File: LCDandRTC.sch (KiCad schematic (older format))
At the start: 13 parts, among them P6 2x8 socket strip, Q3 TSM2314, U2 PCA9306, U3 DS1338, X1 32.768kHz

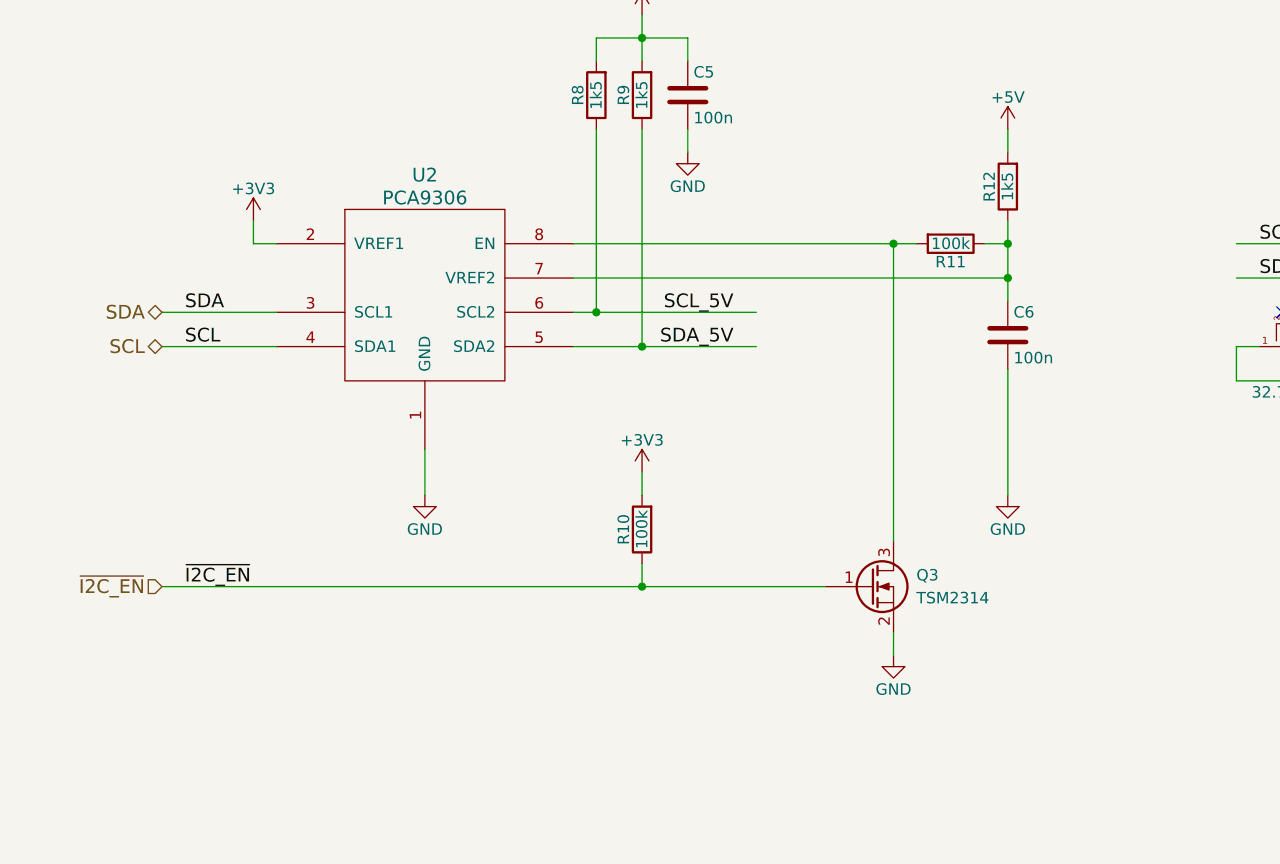
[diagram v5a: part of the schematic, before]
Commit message: Changed layout of I2C buffer enabling
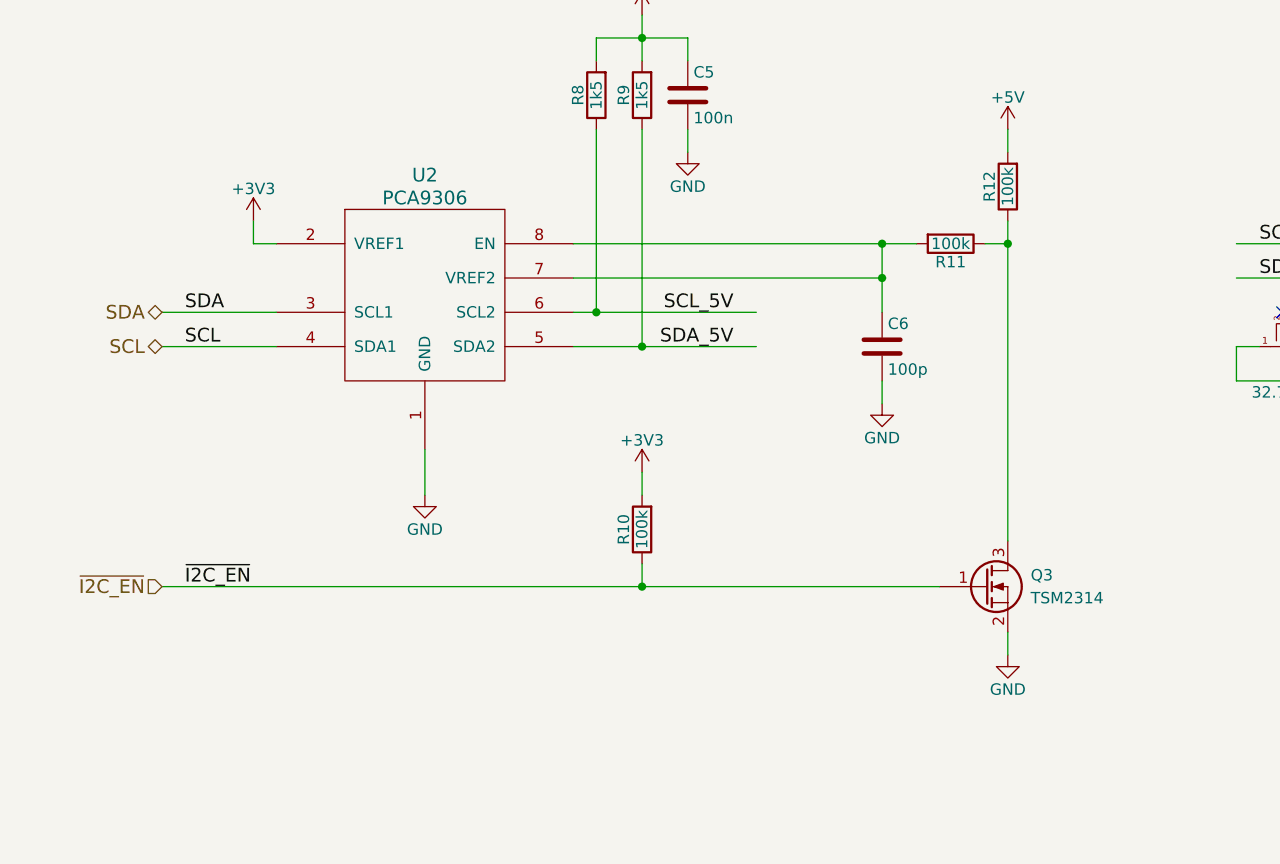
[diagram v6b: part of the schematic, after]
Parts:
- C6: value 100n -> 100p; Alt. Order Code 710-885012207098 -> 810-CGA4C2C0G2A101J; Manufacturer Multicomp -> TDK; Note 100nF/50V X7R 0805 ceramic capacitor -> 100pF/100V C0G(NP0) 0805 ceramic capacitor; Order Code 1759166 -> 2210931; Part Number MC0805B104K250CT -> CGA4C2C0G2A101J060AA
- R12: value 1k5 -> 100k; Alt. Order Code 71-CRCW0805-1.5K-E3 -> 71-CRCW0805-100K-E3; Note 1.5kΩ/1% 0805 resistor -> 100kΩ/1% 0805 resistor; Order Code 2447592 -> 2447551; Part Number MCWR08X1501FTL -> MCWR08X1003FTL
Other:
- moved on the sheet: C6, Q3
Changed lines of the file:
@@
 SCL
 $Comp
-L +3V3 #PWR027
+L +3V3 #PWR27
 U 1 1 566ACC96
 P 3500 1900
-F 0 "#PWR027" H 3500 1750 50  0001 C CNN
+F 0 "#PWR27" H 3500 1750 50  0001 C CNN
 F 1 "+3V3" H 3500 2040 50  0000 C CNN
 F 2 "" H 3500 1900 50  0000 C CNN
@@
 $EndComp
 $Comp
-L +5V #PWR028
+L +5V #PWR35
 U 1 1 566ACCAB
 P 6800 1500
-F 0 "#PWR028" H 6800 1350 50  0001 C CNN
+F 0 "#PWR35" H 6800 1350 50  0001 C CNN
 F 1 "+5V" H 6800 1640 50  0000 C CNN
 F 2 "" H 6800 1500 50  0000 C CNN
@@
 $EndComp
 $Comp
-L GND #PWR029
+L GND #PWR34
 U 1 1 566ACCC2
-P 6800 3100
-F 0 "#PWR029" H 6800 2850 50  0001 C CNN
-F 1 "GND" H 6800 2950 50  0000 C CNN
-F 2 "" H 6800 3100 50  0000 C CNN
-F 3 "" H 6800 3100 50  0000 C CNN
-	1    6800 3100
+P 6250 2700
+F 0 "#PWR34" H 6250 2450 50  0001 C CNN
+F 1 "GND" H 6250 2550 50  0000 C CNN
+F 2 "" H 6250 2700 50  0000 C CNN
+F 3 "" H 6250 2700 50  0000 C CNN
+	1    6250 2700
 	1    0    0    -1
 $EndComp
@@
 L Q_NMOS_GSD Q3
 U 1 1 566ACCC8
-P 6200 3500
-F 0 "Q3" H 6400 3550 50  0000 L CNN
-F 1 "TSM2314" H 6400 3450 50  0000 L CNN
-F 2 "TO_SOT_Packages_SMD:SOT-23" H 6400 3600 50  0001 C CNN
-F 3 "" H 6200 3500 50  0000 C CNN
-F 4 "TSM2314CX" H 6200 3500 60  0001 C CNN "Part Number"
-F 5 "Taiwan Semiconductor" H 6200 3500 60  0001 C CNN "Manufacturer"
-F 6 "SOT-23" H 6200 3500 60  0001 C CNN "Package"
-F 7 "Farnell" H 6200 3500 60  0001 C CNN "Supplier"
-F 8 "1864589" H 6200 3500 60  0001 C CNN "Order Code"
-F 9 "Mouser" H 6200 3500 60  0001 C CNN "Alt. Supplier"
-F 10 "781-SI2314EDS-E3" H 6200 3500 60  0001 C CNN "Alt. Order Code"
-F 11 "N-channel SOT-23 MOSFET" H 6200 3500 60  0001 C CNN "Note"
-	1    6200 3500
-	1    0    0    -1
-$EndComp
-$Comp
-L GND #PWR030
+P 6700 3500
+F 0 "Q3" H 6900 3550 50  0000 L CNN
+F 1 "TSM2314" H 6900 3450 50  0000 L CNN
+F 2 "TO_SOT_Packages_SMD:SOT-23" H 6900 3600 50  0001 C CNN
+F 3 "" H 6700 3500 50  0000 C CNN
+F 4 "TSM2314CX" H 6700 3500 60  0001 C CNN "Part Number"
+F 5 "Taiwan Semiconductor" H 6700 3500 60  0001 C CNN "Manufacturer"
+F 6 "SOT-23" H 6700 3500 60  0001 C CNN "Package"
+F 7 "Farnell" H 6700 3500 60  0001 C CNN "Supplier"
+F 8 "1864589" H 6700 3500 60  0001 C CNN "Order Code"
+F 9 "Mouser" H 6700 3500 60  0001 C CNN "Alt. Supplier"
+F 10 "781-SI2314EDS-E3" H 6700 3500 60  0001 C CNN "Alt. Order Code"
+F 11 "N-channel SOT-23 MOSFET" H 6700 3500 60  0001 C CNN "Note"
+	1    6700 3500
+	1    0    0    -1
+$EndComp
+$Comp
+L GND #PWR29
 U 1 1 566ACCCF
 P 4250 3100
-F 0 "#PWR030" H 4250 2850 50  0001 C CNN
+F 0 "#PWR29" H 4250 2850 50  0001 C CNN
 F 1 "GND" H 4250 2950 50  0000 C CNN
 F 2 "" H 4250 3100 50  0000 C CNN
@@
 $EndComp
 $Comp
-L GND #PWR031
+L GND #PWR36
 U 1 1 566ACCD5
-P 6300 3800
-F 0 "#PWR031" H 6300 3550 50  0001 C CNN
-F 1 "GND" H 6300 3650 50  0000 C CNN
-F 2 "" H 6300 3800 50  0000 C CNN
-F 3 "" H 6300 3800 50  0000 C CNN
-	1    6300 3800
+P 6800 3800
+F 0 "#PWR36" H 6800 3550 50  0001 C CNN
+F 1 "GND" H 6800 3650 50  0000 C CNN
+F 2 "" H 6800 3800 50  0000 C CNN
+F 3 "" H 6800 3800 50  0000 C CNN
+	1    6800 3800
 	1    0    0    -1
 $EndComp
@@
 $EndComp
 $Comp
-L +5V #PWR032
+L +5V #PWR31
 U 1 1 566ACCFE
 P 5200 1000
-F 0 "#PWR032" H 5200 850 50  0001 C CNN
+F 0 "#PWR31" H 5200 850 50  0001 C CNN
 F 1 "+5V" H 5200 1140 50  0000 C CNN
 F 2 "" H 5200 1000 50  0000 C CNN
@@
 $EndComp
 $Comp
-L GND #PWR033
+L GND #PWR33
 U 1 1 566ACD0E
 P 5400 1600
-F 0 "#PWR033" H 5400 1350 50  0001 C CNN
+F 0 "#PWR33" H 5400 1350 50  0001 C CNN
 F 1 "GND" H 5400 1450 50  0000 C CNN
 F 2 "" H 5400 1600 50  0000 C CNN
@@
 LCD_D5
 $Comp
-L GND #PWR034
+L GND #PWR28
 U 1 1 566AD7CE
 P 3750 6100
-F 0 "#PWR034" H 3750 5850 50  0001 C CNN
+F 0 "#PWR28" H 3750 5850 50  0001 C CNN
 F 1 "GND" H 3750 5950 50  0000 C CNN
 F 2 "" H 3750 6100 50  0000 C CNN
@@
 $EndComp
 $Comp
-L +BATT #PWR035
+L +BATT #PWR39
 U 1 1 566ADC91
 P 10100 2450
-F 0 "#PWR035" H 10100 2300 50  0001 C CNN
+F 0 "#PWR39" H 10100 2300 50  0001 C CNN
 F 1 "+BATT" V 10100 2590 50  0000 L CNN
 F 2 "" H 10100 2450 50  0000 C CNN
@@
 $EndComp
 $Comp
-L +3V3 #PWR036
+L +3V3 #PWR32
 U 1 1 566B2C19
 P 5200 3000
-F 0 "#PWR036" H 5200 2850 50  0001 C CNN
+F 0 "#PWR32" H 5200 2850 50  0001 C CNN
 F 1 "+3V3" H 5200 3140 50  0000 C CNN
 F 2 "" H 5200 3000 50  0000 C CNN
@@
 NoConn ~ 9900 2150
 $Comp
-L +12V #PWR037
+L +12V #PWR30
 U 1 1 566AAE29
 P 4650 5200
-F 0 "#PWR037" H 4650 5050 50  0001 C CNN
+F 0 "#PWR30" H 4650 5050 50  0001 C CNN
 F 1 "+12V" H 4650 5340 50  0000 C CNN
 F 2 "" H 4650 5200 50  0000 C CNN
@@
 	3500 2000 3500 1900
 Wire Wire Line
-	6800 2150 4900 2150
-Wire Wire Line
-	6800 1900 6800 2250
-Wire Wire Line
-	4900 2000 6400 2000
-Wire Wire Line
-	6700 2000 6800 2000
-Connection ~ 6800 2000
-Wire Wire Line
 	6800 1500 6800 1600
-Connection ~ 6800 2150
-Wire Wire Line
-	6800 2550 6800 3100
+Wire Wire Line
+	6250 2600 6250 2700
 Wire Wire Line
 	4250 2900 4250 3100
 Wire Wire Line
-	6300 3700 6300 3800
-Wire Wire Line
-	6300 3300 6300 2000
-Connection ~ 6300 2000
-Wire Wire Line
-	3100 3500 6000 3500
+	6800 3700 6800 3800
+Wire Wire Line
+	3100 3500 6500 3500
 Wire Wire Line
 	4900 2300 5700 2300
@@
 	9100 1550 9100 1300
 $Comp
-L +5V #PWR038
+L +5V #PWR37
 U 1 1 56700AB7
 P 9100 1300
-F 0 "#PWR038" H 9100 1150 50  0001 C CNN
+F 0 "#PWR37" H 9100 1150 50  0001 C CNN
 F 1 "+5V" H 9100 1440 50  0000 C CNN
 F 2 "" H 9100 1300 50  0000 C CNN
@@
 $EndComp
 $Comp
-L GND #PWR039
+L GND #PWR38
 U 1 1 56700B0D
 P 9100 3300
-F 0 "#PWR039" H 9100 3050 50  0001 C CNN
+F 0 "#PWR38" H 9100 3050 50  0001 C CNN
 F 1 "GND" H 9100 3150 50  0000 C CNN
 F 2 "" H 9100 3300 50  0000 C CNN
@@
 L C C6
 U 1 1 567547AA
-P 6800 2400
-F 0 "C6" H 6825 2500 50  0000 L CNN
-F 1 "100n" H 6825 2300 50  0000 L CNN
-F 2 "Capacitors_SMD:C_0805" H 6838 2250 50  0001 C CNN
-F 3 "" H 6800 2400 50  0000 C CNN
-F 4 "MC0805B104K250CT" H 6800 2400 60  0001 C CNN "Part Number"
-F 5 "Multicomp" H 6800 2400 60  0001 C CNN "Manufacturer"
-F 6 "0805" H 6800 2400 60  0001 C CNN "Package"
-F 7 "Farnell" H 6800 2400 60  0001 C CNN "Supplier"
-F 8 "1759166" H 6800 2400 60  0001 C CNN "Order Code"
-F 9 "Mouser" H 6800 2400 60  0001 C CNN "Alt. Supplier"
-F 10 "710-885012207098" H 6800 2400 60  0001 C CNN "Alt. Order Code"
-F 11 "100nF/50V X7R 0805 ceramic capacitor" H 6800 2400 60  0001 C CNN "Note"
-	1    6800 2400
+P 6250 2450
+F 0 "C6" H 6275 2550 50  0000 L CNN
+F 1 "100p" H 6275 2350 50  0000 L CNN
+F 2 "Capacitors_SMD:C_0805" H 6288 2300 50  0001 C CNN
+F 3 "" H 6250 2450 50  0000 C CNN
+F 4 "CGA4C2C0G2A101J060AA" H 6250 2450 60  0001 C CNN "Part Number"
+F 5 "TDK" H 6250 2450 60  0001 C CNN "Manufacturer"
+F 6 "0805" H 6250 2450 60  0001 C CNN "Package"
+F 7 "Farnell" H 6250 2450 60  0001 C CNN "Supplier"
+F 8 "2210931" H 6250 2450 60  0001 C CNN "Order Code"
+F 9 "Mouser" H 6250 2450 60  0001 C CNN "Alt. Supplier"
+F 10 "810-CGA4C2C0G2A101J" H 6250 2450 60  0001 C CNN "Alt. Order Code"
+F 11 "100pF/100V C0G(NP0) 0805 ceramic capacitor" H 6250 2450 60  0001 C CNN "Note"
+	1    6250 2450
 	1    0    0    -1
 $EndComp
@@
 	-1   0    0    1
 $EndComp
+Wire Wire Line
+	4900 2000 6400 2000
+Wire Wire Line
+	6250 2000 6250 2300
+Connection ~ 6250 2000
+Wire Wire Line
+	4900 2150 6250 2150
+Wire Wire Line
+	6800 1900 6800 3300
+Connection ~ 6250 2150
+Wire Wire Line
+	6700 2000 6800 2000
+Connection ~ 6800 2000
 $Comp
 L R R12
-U 1 1 56754D8D
+U 1 1 56EC826B
 P 6800 1750
 F 0 "R12" V 6880 1750 50  0000 C CNN
-F 1 "1k5" V 6800 1750 50  0000 C CNN
+F 1 "100k" V 6800 1750 50  0000 C CNN
 F 2 "Resistors_SMD:R_0805" V 6730 1750 50  0001 C CNN
 F 3 "" H 6800 1750 50  0000 C CNN
-F 4 "MCWR08X1501FTL" V 6800 1750 60  0001 C CNN "Part Number"
+F 4 "MCWR08X1003FTL" V 6800 1750 60  0001 C CNN "Part Number"
 F 5 "Multicomp" V 6800 1750 60  0001 C CNN "Manufacturer"
 F 6 "0805" H 6800 1750 60  0001 C CNN "Package"
 F 7 "Farnell" H 6800 1750 60  0001 C CNN "Supplier"
-F 8 "2447592" V 6800 1750 60  0001 C CNN "Order Code"
+F 8 "2447551" V 6800 1750 60  0001 C CNN "Order Code"
 F 9 "Mouser" H 6800 1750 60  0001 C CNN "Alt. Supplier"
-F 10 "71-CRCW0805-1.5K-E3" H 6800 1750 60  0001 C CNN "Alt. Order Code"
-F 11 "1.5kΩ/1% 0805 resistor" H 6800 1750 60  0001 C CNN "Note"
+F 10 "71-CRCW0805-100K-E3" H 6800 1750 60  0001 C CNN "Alt. Order Code"
+F 11 "100kΩ/1% 0805 resistor" H 6800 1750 60  0001 C CNN "Note"
 	1    6800 1750
 	-1   0    0    1
